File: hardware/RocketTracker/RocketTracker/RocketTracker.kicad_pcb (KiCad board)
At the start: 2 copper layers, 25 x 35 mm, 61 parts, among them J201 LiPo, Q101 AO3400A, SW201 Power Switch, SW301 BOOT_sw, SW302 RESET_sw, U201 MCP73871-1CC, U202 TPS63070RNMR, U301 ESP32-C3-WROOM-02

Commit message: 帰宅
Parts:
- moved R103 0.30 mm to (88.4, 80.4)
- moved R104 0.30 mm to (88.4, 81.4)
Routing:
- net VPP: track 0.00 -> 26.8 mm, vias 0 -> 2
- net Net-(U202-L2): track 0.00 -> 13.4 mm, vias 0 -> 6
- net Net-(U202-L1): track 0.00 -> 13.2 mm, vias 0 -> 6
- net Net-(U202-VIN): track 8.42 -> 16.6 mm
- net Net-(U201-THERM): track 0.00 -> 4.75 mm
- net Net-(J201-Pin_1): track 0.00 -> 3.94 mm
- net Net-(LED201-K): track 0.00 -> 2.03 mm
- net Net-(U201-PROG1): track 0.00 -> 1.27 mm
- net Net-(U201-PROG3): track 0.00 -> 1.24 mm

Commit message: ガーバー出力
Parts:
- moved R102 1.50 mm to (96.2, 60.8), turned to 90 degrees
- moved R209 0.53 mm to (94.1, 77.2)
- moved R206 0.22 mm to (98.1, 71.5)
- moved C201 0.20 mm to (98.2, 74.0)
- moved R208 0.10 mm to (105.1, 73.4)
- moved R210 0.10 mm to (105.1, 74.4)
- moved R213 0.10 mm to (94.0, 71.0)
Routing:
- net GND: track 0.00 -> 61.2 mm, vias 0 -> 31
- net VDD: track 16.8 -> 70.3 mm, vias 0 -> 5
- net /ESP32C3core/IO1: track 0.00 -> 35.0 mm, vias 0 -> 1
- net Net-(U301-EN): track 0.00 -> 35.0 mm, vias 0 -> 3
- net /ESP32C3core/IO0: track 0.00 -> 33.6 mm, vias 0 -> 1
- net Net-(U301-IO9): track 0.00 -> 22.1 mm, vias 0 -> 2
- net Net-(SW201-C): track 0.00 -> 16.7 mm, vias 0 -> 2
- net /ESP32C3core/IO10: track 0.00 -> 15.4 mm, vias 0 -> 1
- net Net-(SW201-B): track 0.00 -> 4.64 mm
- net Net-(LED201-A): track 14.9 -> 18.9 mm, vias 0 -> 2
- net Net-(LED202-A): track 0.00 -> 3.81 mm
- net Net-(LED203-A): track 0.00 -> 3.63 mm, vias 0 -> 2
- net Net-(LED203-K): track 0.00 -> 3.57 mm
- net Net-(BZ101--): track 0.00 -> 2.79 mm
- net Net-(U202-VIN): track 16.6 -> 18.9 mm
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- added copper zone on B.Cu, net GND
- added copper zone on F.Cu, net GND
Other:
- board size 25 x 35 mm -> 27 x 35 mm

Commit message: シルク入れた
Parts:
- LED201: value USB Power -> USB
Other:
- board size 27 x 35 mm -> 27 x 35.5 mm
- board text added: "Created by WOBC"
- board text added: "WASA_Rocket RocketTracker"
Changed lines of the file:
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@@
 		)
 		(property "Value" "FULL"
-			(at 0 1.65 90)
-			(layer "F.Fab")
+			(at 3 -0.7 90)
+			(layer "F.SilkS")
 			(effects
 				(font
@@
 		)
 		(property "Value" "VDD"
-			(at 0 1.65 0)
-			(layer "F.Fab")
+			(at 1 1.7 0)
+			(layer "F.SilkS")
 			(effects
 				(font
@@
 		)
 		(property "Value" "STAT"
-			(at 0 1.65 0)
-			(layer "F.Fab")
+			(at -0.5 1.8 0)
+			(layer "F.SilkS")
 			(effects
 				(font
@@
 			)
 		)
-		(property "Value" "USB Power"
-			(at 0 1.65 90)
-			(layer "F.Fab")
+		(property "Value" "USB"
+			(at -1.1 -5.8 180)
+			(layer "F.SilkS")
 			(effects
 				(font
@@
 		)
 		(property "Value" "ERROR"
-			(at 0 1.65 0)
-			(layer "F.Fab")
+			(at -0.6 -1.6 0)
+			(layer "F.SilkS")
 			(effects
 				(font
@@
 		(tags "Diode SOD882 DFN1006-2")
 		(property "Reference" "D303"
-			(at 5.75 -14.8 90)
+			(at 9.4 -25.2 90)
 			(layer "F.SilkS")
 			(effects
@@
 		)
 		(property "Value" "CHARGE"
-			(at 0 1.65 90)
-			(layer "F.Fab")
+			(at 4.6 0.8 90)
+			(layer "F.SilkS")
 			(effects
 				(font
@@
 		(at 93.472 86.614)
 		(property "Reference" "USB301"
-			(at 13.728 2.786 0)
+			(at 24.128 7.086 0)
 			(unlocked yes)
 			(layer "F.SilkS")
@@
 		(sheetfile "RocketTracker.kicad_sch")
 		(fp_line
-			(start -13.5 16.5)
+			(start -13.5 17.000001)
 			(end -13.5 -11.5)
 			(stroke
@@
 		)
 		(fp_line
-			(start 10 20)
-			(end -10.000001 20)
+			(start 10 20.5)
+			(end -10.000001 20.5)
 			(stroke
 				(width 0.05)
@@
 		(fp_line
 			(start 13.5 -11.5)
-			(end 13.5 16.5)
+			(end 13.5 17)
 			(stroke
 				(width 0.05)
@@
 		)
 		(fp_arc
-			(start -10 20)
-			(mid -12.474874 18.974874)
-			(end -13.5 16.5)
+			(start -10 20.5)
+			(mid -12.474874 19.474874)
+			(end -13.5 17)
 			(stroke
 				(width 0.05)
@@
 		)
 		(fp_arc
-			(start 13.5 16.5)
-			(mid 12.474874 18.974874)
-			(end 10 20)
+			(start 13.5 17)
+			(mid 12.474874 19.474874)
+			(end 10 20.5)
 			(stroke
 				(width 0.05)
@@
 		(tags "ESP32-C3 WROOM-02 espressif")
 		(property "Reference" "U301"
-			(at -10.5 -5.13 90)
+			(at -32.134 -3.89 90)
 			(layer "B.SilkS")
 			(effects
@@
 		)
 	)
+	(gr_line
+		(start 95.4 78.6)
+		(end 98.4 78.4)
+		(stroke
+			(width 0.1)
+			(type default)
+		)
+		(layer "F.SilkS")
+	)
+	(gr_text "Created by WOBC"
+		(at 100 80.3 0)
+		(layer "B.SilkS")
+		(effects
+			(font
+				(size 1 1)
+				(thickness 0.1)
+			)
+			(justify left bottom mirror)
+		)
+	)
+	(gr_text "WASA_Rocket\nRocketTracker"
+		(at 100.1 78.9 0)
+		(layer "B.SilkS")
+		(effects
+			(font
+				(size 1.2 1.2)
+				(thickness 0.15)
+			)
+			(justify left bottom mirror)
+		)
+	)

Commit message: 軽微な修正
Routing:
- net GND: track 61.2 -> 61.5 mm, vias 31 -> 91
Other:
- board text added: "Designed by M.Numata N.Tajima O.Morita Y.Hara"

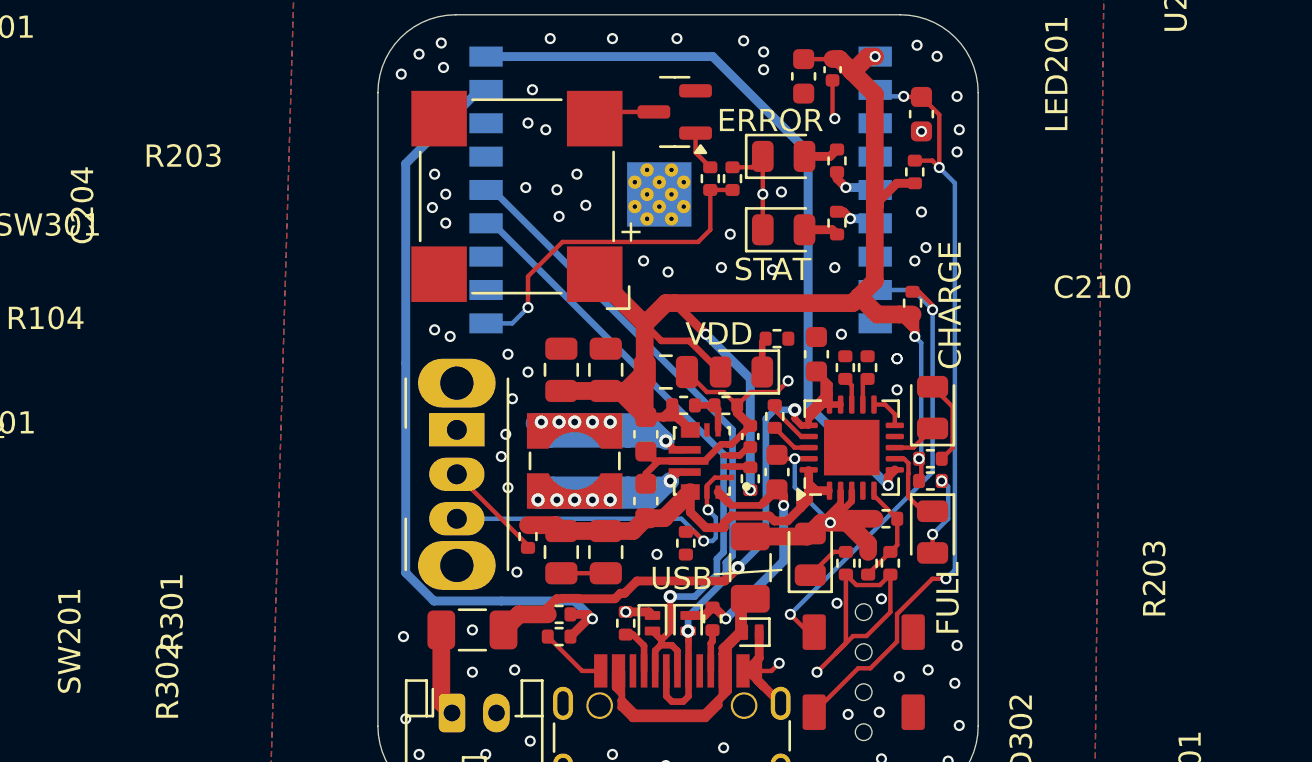
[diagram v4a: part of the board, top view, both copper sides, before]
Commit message: 充電ICのTHERMピンへの入力変更
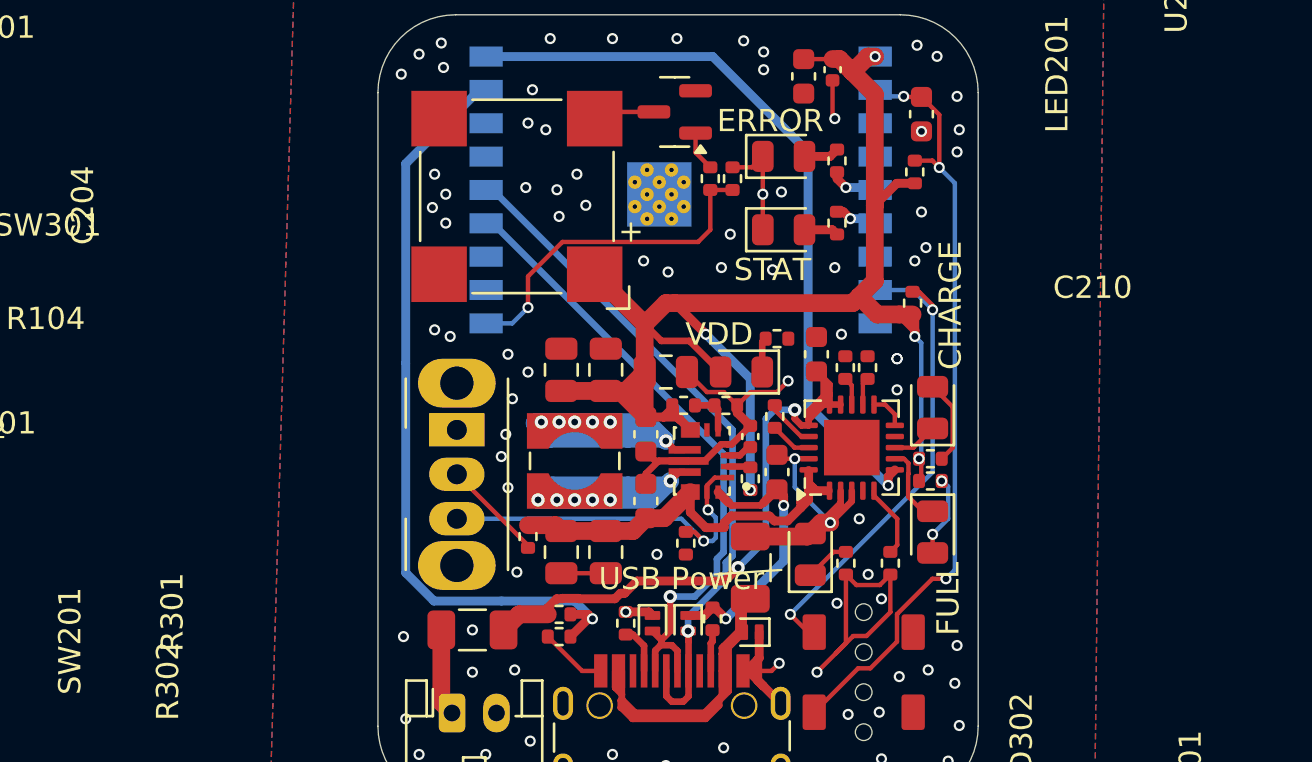
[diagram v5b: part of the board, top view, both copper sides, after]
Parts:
- removed R203 (x2): 10k, Resistor_SMD:R_0402_1005Metric
- LED201: value USB -> USB Power
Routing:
- net Net-(LED201-A): track 18.9 -> 15.1 mm
- net Net-(U201-THERM): track 4.75 -> 3.31 mm
- net GND: vias 91 -> 93

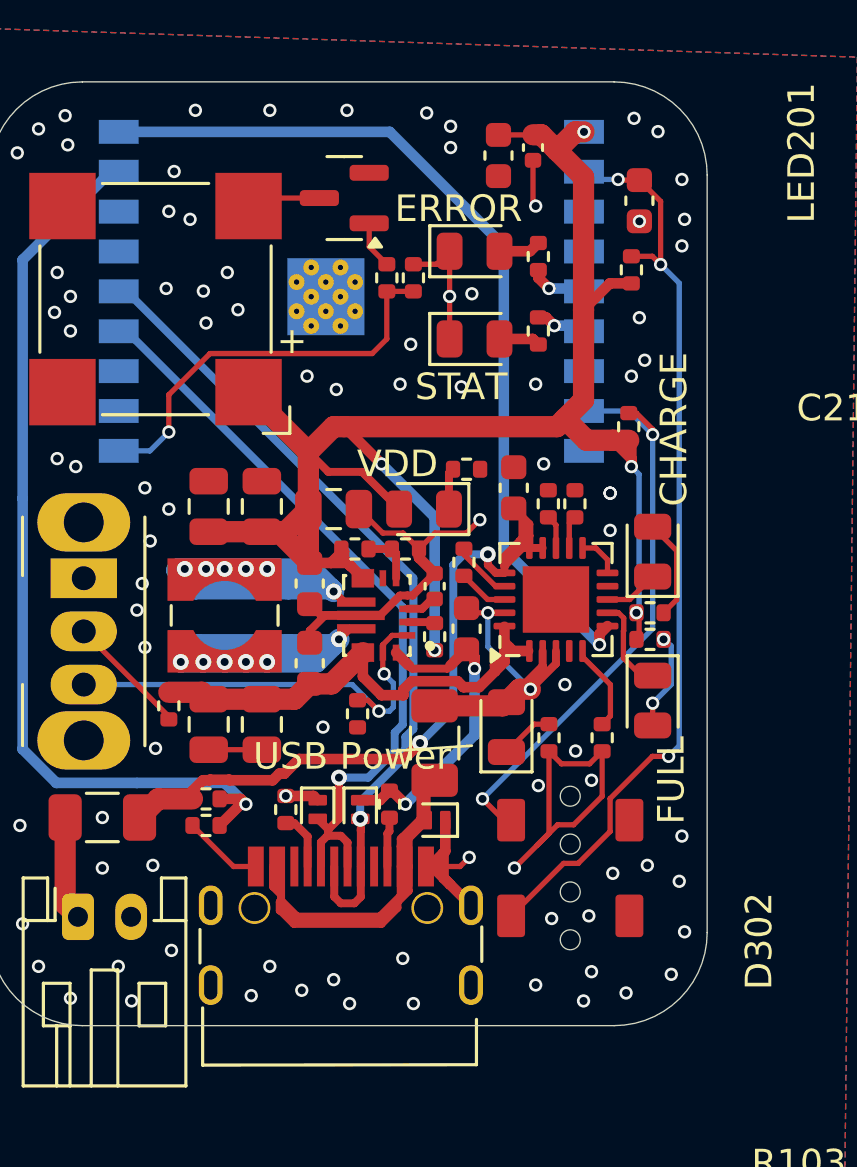
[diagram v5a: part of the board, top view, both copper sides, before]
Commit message: スイッチのシルク追加
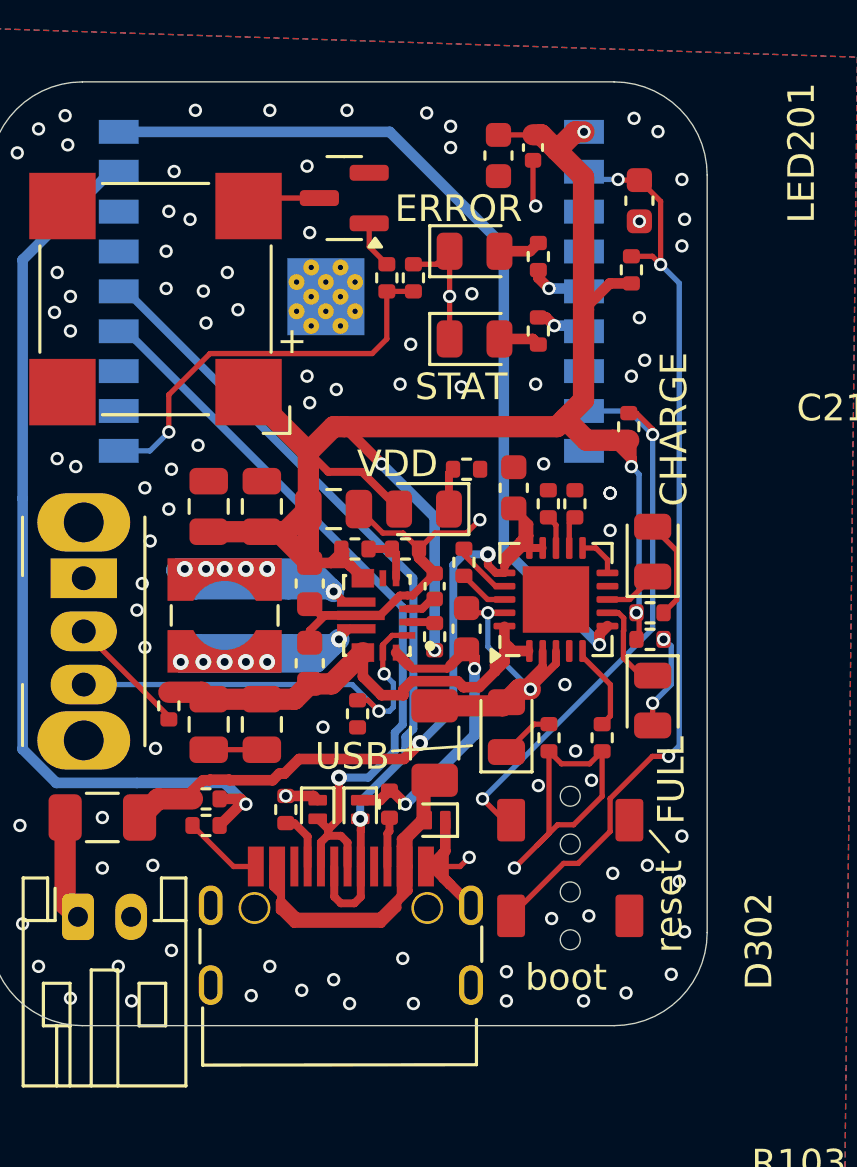
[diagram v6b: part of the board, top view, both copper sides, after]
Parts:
- LED201: value USB Power -> USB
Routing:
- net GND: vias 93 -> 99
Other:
- board text added: "boot"
- board text added: "reset"
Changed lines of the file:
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@@
 			)
 		)
-		(property "Value" "USB Power"
+		(property "Value" "USB"
 			(at -1.1 -5.8 180)
 			(layer "F.SilkS")
@@
 		(layer "F.SilkS")
 	)
+	(gr_line
+		(start 105.1 81.6)
+		(end 105.8 82.4)
+		(stroke
+			(width 0.1)
+			(type default)
+		)
+		(layer "F.SilkS")
+	)
+	(gr_text "reset"
+		(at 106.4 86.2 90)
+		(layer "F.SilkS")
+		(effects
+			(font
+				(size 1 1)
+				(thickness 0.1)
+			)
+			(justify left bottom)
+		)
+	)
+	(gr_text "boot"
+		(at 100.4 87.7 0)
+		(layer "F.SilkS")
+		(effects
+			(font
+				(size 1 1)
+				(thickness 0.1)
+			)
+			(justify left bottom)
+		)
+	)
 	(gr_text "Designed by\nM.Numata\nN.Tajima\nO.Morita\nY.Hara"
 		(at 95.1 83.7 0)
@@
 	)
 	(via
+		(at 87.1 68)
+		(size 0.5)
+		(drill 0.3)
+		(layers "F.Cu" "B.Cu")
+		(free yes)
+		(net 1)
+	)
+	(via
 		(at 101.1 67.8)
 		(size 0.5)
@@
 	)
 	(via
-		(at 102.9 86.9)
+		(at 99.7 88)
 		(size 0.5)
 		(drill 0.3)
@@
 	)
 	(via
+		(at 88.1 67.1)
+		(size 0.5)
+		(drill 0.3)
+		(layers "F.Cu" "B.Cu")
+		(free yes)
+		(net 1)
+	)
+	(via
 		(at 86.3 70.7)
 		(size 0.5)
@@
 	)
 	(via
+		(at 92.3 59.1)
+		(size 0.5)
+		(drill 0.3)
+		(layers "F.Cu" "B.Cu")
+		(free yes)
+		(net 1)
+	)
+	(via
 		(at 106.2 83.5)
 		(size 0.5)
@@
 	)
 	(via
+		(at 86.9 59.8)
+		(size 0.5)
+		(drill 0.3)
+		(layers "F.Cu" "B.Cu")
+		(free yes)
+		(net 1)
+	)
+	(via
 		(at 88.4 62.5)
 		(size 0.5)
@@
 	)
 	(via
+		(at 92.2 56.6)
+		(size 0.5)
+		(drill 0.3)
+		(layers "F.Cu" "B.Cu")
+		(free yes)
+		(net 1)
+	)
+	(via
 		(at 97.6 55.9)
 		(size 0.5)
@@
 	)
 	(via
-		(at 100.8 87.4)
+		(at 99.7 86.9)
 		(size 0.5)
 		(drill 0.3)
@@
 		(size 0.5)
 		(drill 0.3)
+		(layers "F.Cu" "B.Cu")
+		(free yes)
+		(net 1)
+	)
+	(via
+		(at 92.3 65.5)
+		(size 0.5)
+		(drill 0.3)

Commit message: コンデンサ，ダイオード追加
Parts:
- removed R104: 10k, Resistor_SMD:R_0402_1005Metric
- added C211: 22uF, Capacitor_SMD:C_0805_2012Metric, F.Cu at (85.6, 67.2)
- added D201: D, Diode_SMD:D_SOD-323, F.Cu at (86.9, 55.4)
- added R203: 100k, Resistor_SMD:R_0402_1005Metric, F.Cu at (88.4, 81.4)
- LED201: value USB -> USB Power
- R103: value 10k -> 100k
- moved BZ101 0.70 mm to (86.5, 60.9)
- turned R102 to -90 degrees
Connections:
- BZ101 pad 1: VDD -> /LiPo/MCPOUT
- C202 pad 1: Net-(U202-VIN) -> /LiPo/MCPOUT
- C203 pad 1: Net-(U202-VIN) -> /LiPo/MCPOUT
- C205 pad 1: Net-(U202-VIN) -> /LiPo/MCPOUT
- R102 pad 1: /ESP32C3core/IO10 -> Net-(Q101-G)
- R207 pad 1: Net-(U202-VIN) -> /LiPo/MCPOUT
- U201 pad 1: Net-(U202-VIN) -> /LiPo/MCPOUT
- U201 pad 20: Net-(U202-VIN) -> /LiPo/MCPOUT
- U202 pad 12_13: Net-(U202-VIN) -> /LiPo/MCPOUT
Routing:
- net /LiPo/MCPOUT: track 0.00 -> 45.0 mm, vias 0 -> 2
- net Net-(U202-VIN): track 18.9 -> 0.00 mm
- net GND: track 61.5 -> 69.4 mm, vias 99 -> 94
- net VDD: track 70.3 -> 67.1 mm
- net Net-(BZ101--): track 2.79 -> 5.67 mm
- net Net-(Q101-G): track 1.81 -> 2.81 mm

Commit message: 発注！
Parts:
- removed B101: ~, WOBCLibrary:Board_1U_60x60
- removed D301, D302, D303: 5V, Diode_SMD:D_SOD-882
- added U203: USBLC6-2SC6, Package_TO_SOT_SMD:SOT-23-6, F.Cu at (93.3, 79.8)
- LED201: value USB Power -> USB
- moved R301 0.90 mm to (90.5, 80.8)
- moved F201 0.58 mm to (97.5, 78.6)
- moved R209 0.22 mm to (94.0, 77.0), turned to 180 degrees
- moved R302 0.22 mm to (95.5, 80.7)
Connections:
- USB301 pad A6: /ESP32C3core/USB_D+ -> Net-(U203-I/O2-Pad3)
- USB301 pad A7: /ESP32C3core/USB_D- -> Net-(U203-I/O1-Pad1)
- USB301 pad B6: /ESP32C3core/USB_D+ -> Net-(U203-I/O2-Pad3)
- USB301 pad B7: /ESP32C3core/USB_D- -> Net-(U203-I/O1-Pad1)
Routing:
- net /ESP32C3core/USB_D+: track 30.8 -> 23.7 mm
- net GND: track 69.4 -> 76.1 mm, vias 94 -> 92
- net /ESP32C3core/USB_D-: track 29.0 -> 23.4 mm
- net Net-(U203-I/O2-Pad3): track 0.00 -> 5.50 mm
- net /ESP32C3core/VUSB: track 25.0 -> 30.0 mm
- net Net-(U203-I/O1-Pad1): track 0.00 -> 4.18 mm
- net VPP: track 28.5 -> 29.5 mm
- net /ESP32C3core/IO1: track 35.0 -> 34.1 mm
- net Net-(USB301-CC1): track 2.16 -> 2.88 mm
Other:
- outline, holes or cut-outs redrawn
